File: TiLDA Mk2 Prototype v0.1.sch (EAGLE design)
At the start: 196 parts, among them IC1 ATSAM3X8EA-AU, IC10 MCP73831, IC2 MPU-6050, IC3 SRF-V1.2, IC5 S25FL216K0PMFI011, IC7 HMC5883LSMD (NP), IC8 MCP1825T-3302E/DC, IC9 TC1015-3V3, J1 ZX62-AB-5PA(11), J3 Arduino Headers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

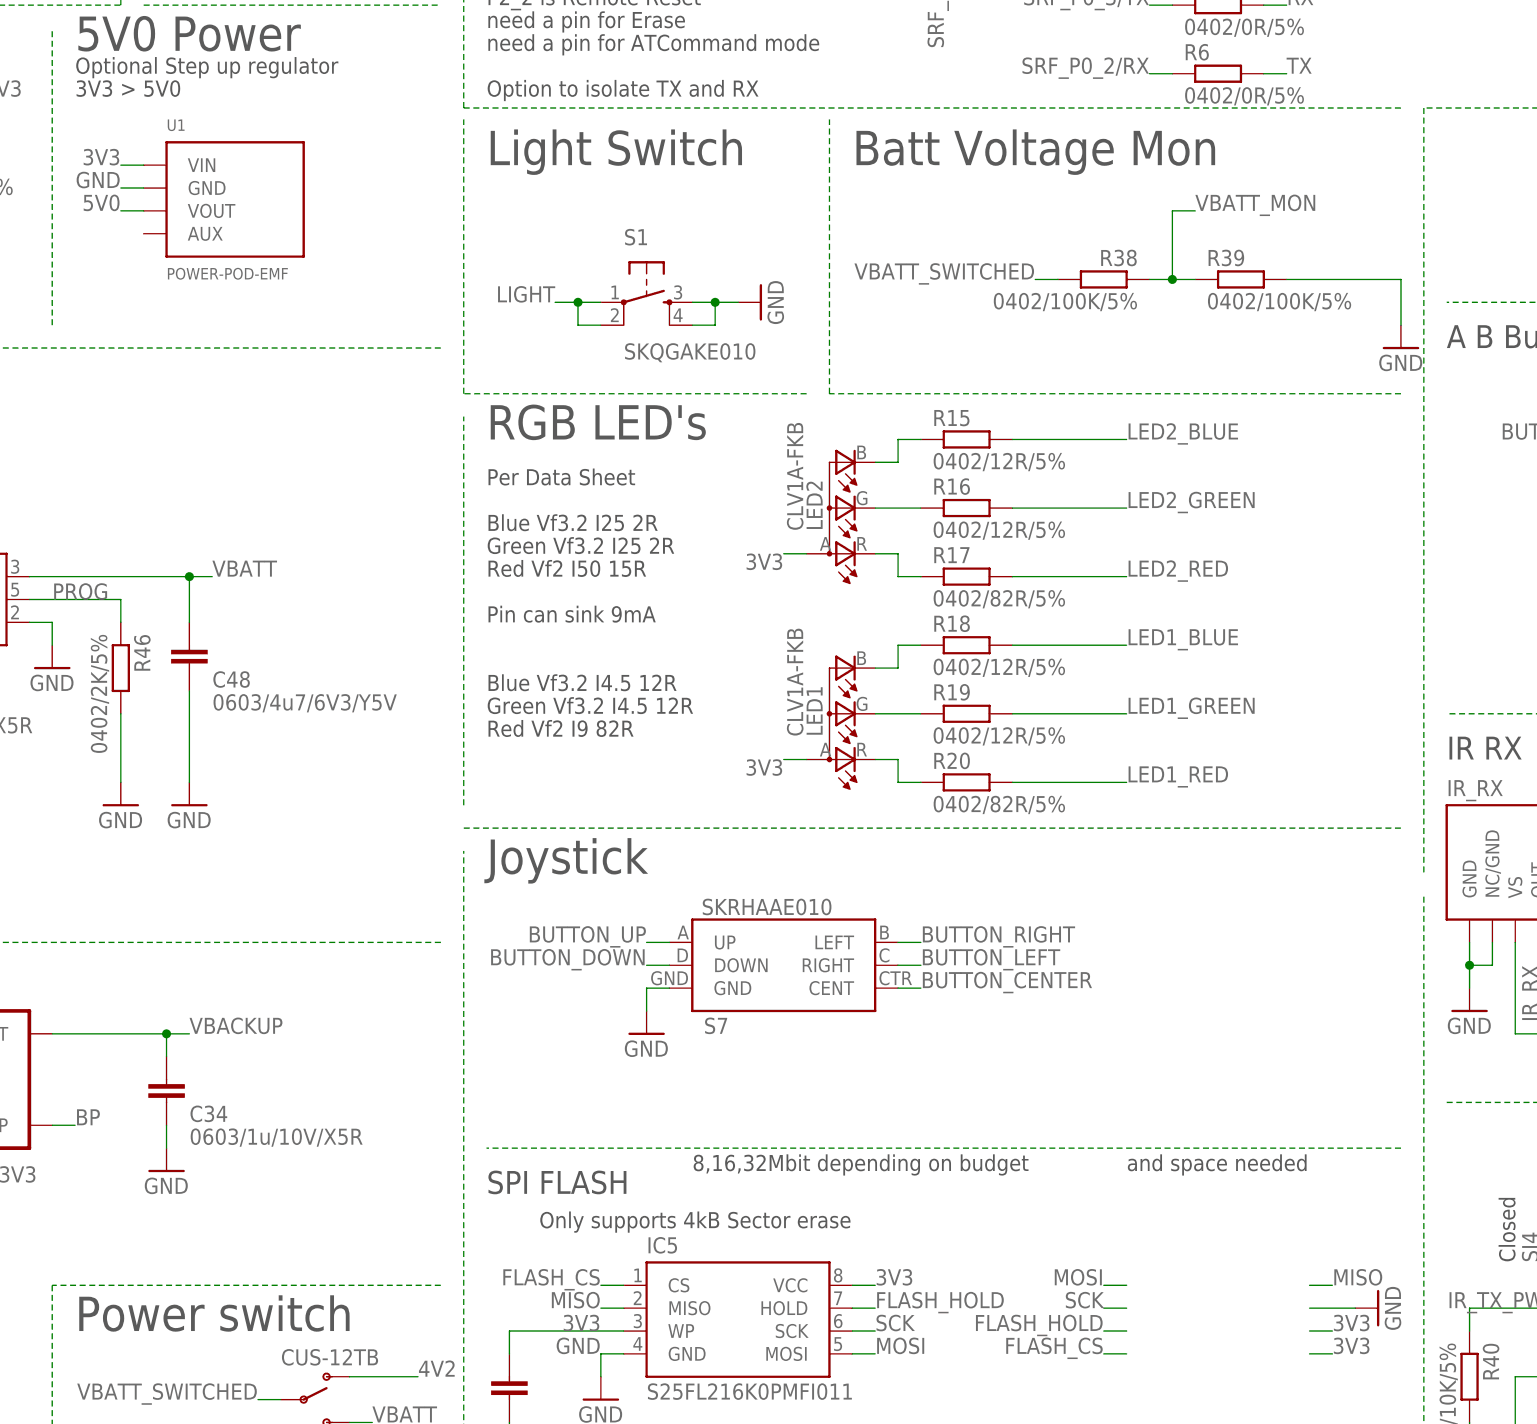
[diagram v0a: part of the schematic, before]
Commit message: Prototype: Last tweak for v0.2, adding SJ for VDDIO between 3V3 and VBACKUP
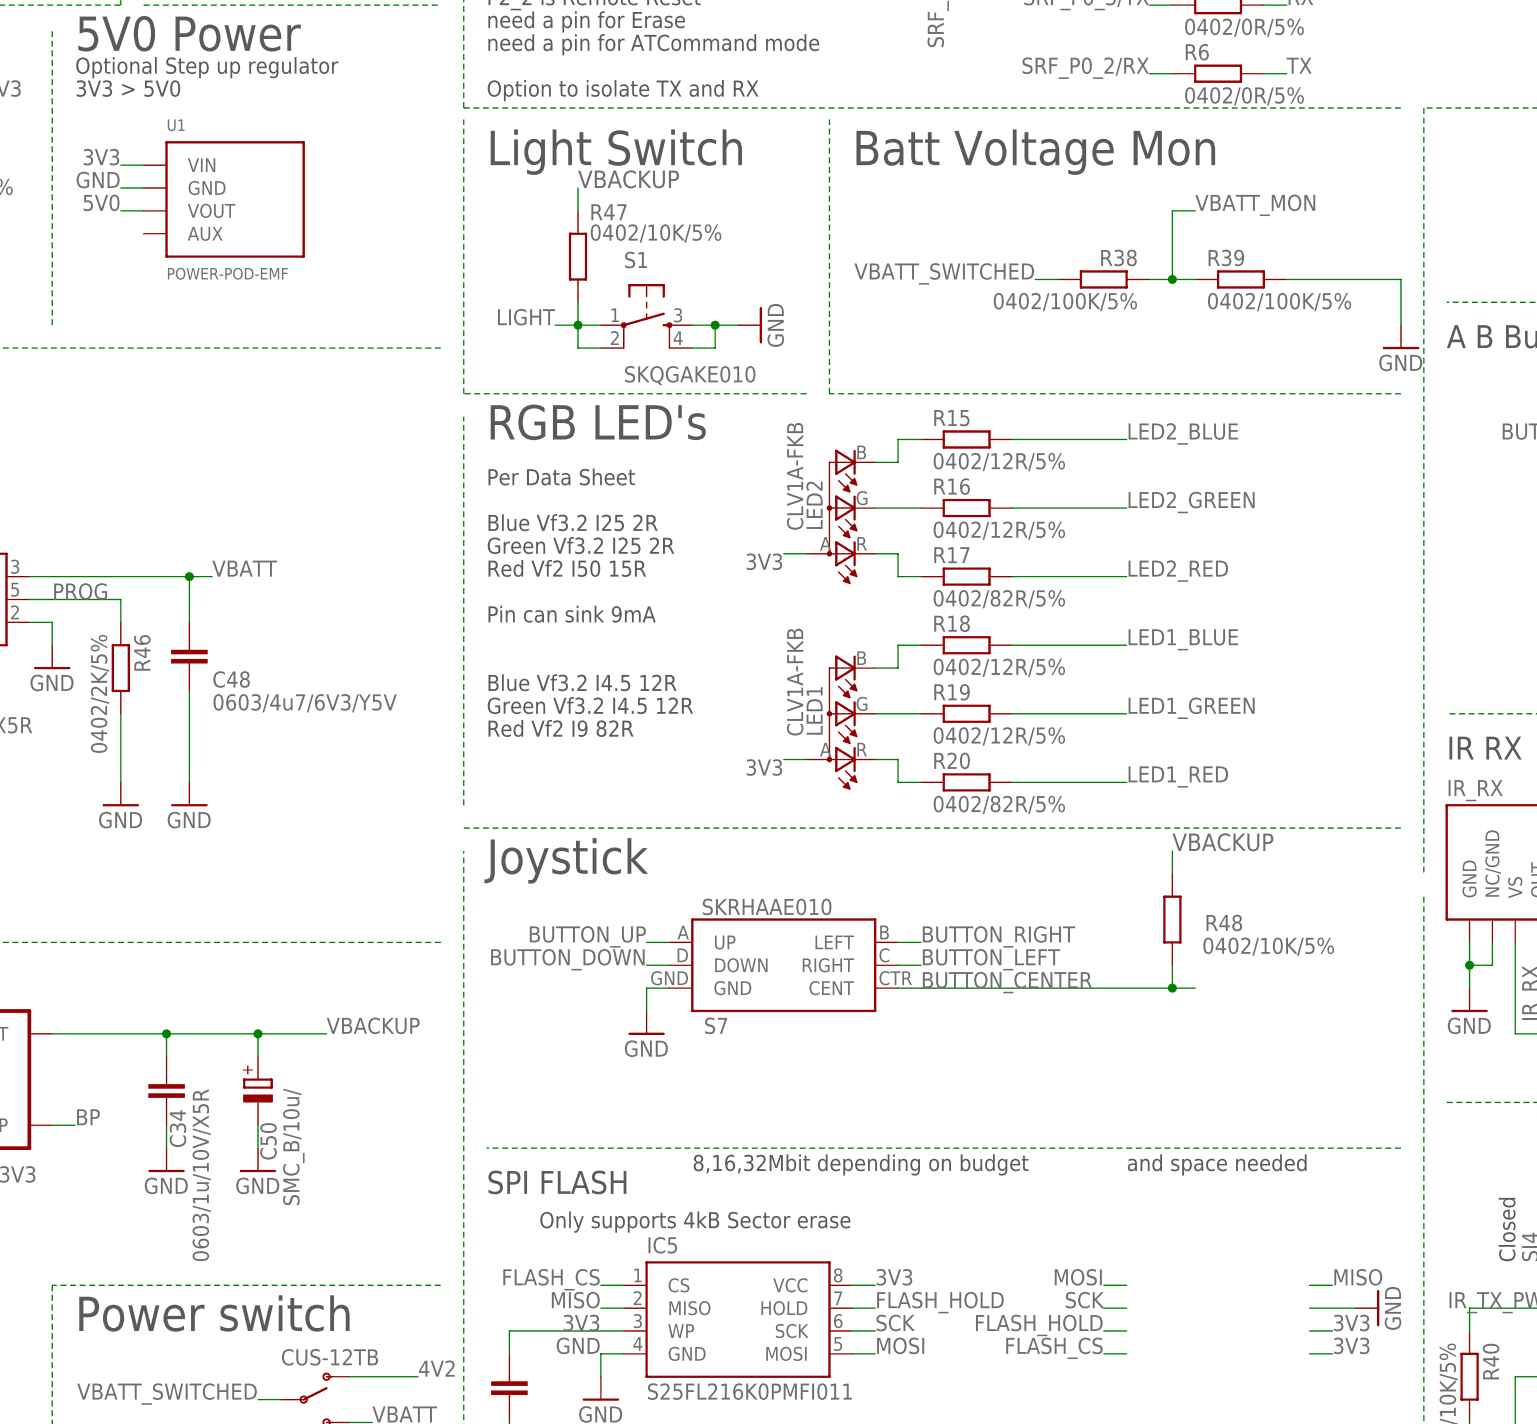
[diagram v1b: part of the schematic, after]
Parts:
- added C50: SMC_B/10u/, TiLDA Mk2 Parts:CPOL-EU-C0805RNDPOL
- added R47, R48: 0402/10K/5%, TiLDA Mk2 Parts:R-EU_R0402-ARDUINO-ROUND
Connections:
- net BUTTON_CENTER: now also R48.1
- net GND: now also C50.-
- net LIGHT: now also R47.1
- net VBACKUP: now also C50.+, R47.2, R48.2
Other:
- moved on the sheet: S1
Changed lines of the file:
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@@
 </part>
 <part name="U1" library="TiLDA Mk2 Parts" deviceset="POWER-POD" device="-EMF"/>
+<part name="R47" library="TiLDA Mk2 Parts" deviceset="R-EU_" device="R0402-ARDUINO-ROUND" value="0402/10K/5%"/>
+<part name="R48" library="TiLDA Mk2 Parts" deviceset="R-EU_" device="R0402-ARDUINO-ROUND" value="0402/10K/5%"/>
+<part name="C50" library="TiLDA Mk2 Parts" deviceset="CPOL-EU" device="-C0805RNDPOL" value="SMC_B/10u/"/>
+<part name="GND9" library="TiLDA Mk2 Parts" deviceset="GND" device=""/>
 </parts>
 <sheets>
@@
 <attribute name="VALUE" x="561.34" y="132.08" size="1.778" layer="94"/>
 </instance>
-<instance part="S1" gate="S" x="134.62" y="134.62"/>
+<instance part="S1" gate="S" x="134.62" y="132.08"/>
 <instance part="S4" gate="S" x="426.72" y="185.42"/>
 <instance part="FRAME2" gate="G$1" x="401.32" y="0"/>
@@
 </instance>
 <instance part="GND41" gate="1" x="439.42" y="185.42" rot="R90"/>
-<instance part="GND42" gate="1" x="147.32" y="134.62" rot="R90"/>
+<instance part="GND42" gate="1" x="147.32" y="132.08" rot="R90"/>
 <instance part="GND43" gate="1" x="375.92" y="121.92" rot="R90"/>
 <instance part="GND44" gate="1" x="375.92" y="106.68" rot="R90"/>
@@
 </instance>
 <instance part="C34" gate="G$1" x="81.28" y="45.72" smashed="yes" rot="R180">
-<attribute name="NAME" x="83.82" y="43.561" size="1.778" layer="95"/>
-<attribute name="VALUE" x="83.82" y="41.021" size="1.778" layer="96"/>
+<attribute name="NAME" x="83.439" y="40.64" size="1.778" layer="95" rot="R90"/>
+<attribute name="VALUE" x="85.979" y="27.94" size="1.778" layer="96" rot="R90"/>
 </instance>
 <instance part="GND63" gate="1" x="35.56" y="35.56"/>
@@
 <instance part="TP26" gate="G$1" x="670.56" y="182.88" rot="R270"/>
 <instance part="U1" gate="G$1" x="88.9" y="144.78"/>
+<instance part="R47" gate="G$1" x="127" y="139.7" smashed="yes" rot="R90">
+<attribute name="NAME" x="128.27" y="143.7386" size="1.778" layer="95"/>
+<attribute name="VALUE" x="128.27" y="141.478" size="1.778" layer="96"/>
+</instance>
+<instance part="R48" gate="G$1" x="193.04" y="66.04" smashed="yes" rot="R90">
+<attribute name="NAME" x="196.6214" y="64.77" size="1.778" layer="95"/>
+<attribute name="VALUE" x="196.342" y="62.23" size="1.778" layer="96"/>
+</instance>
+<instance part="C50" gate="G$1" x="91.44" y="48.26" smashed="yes">
+<attribute name="NAME" x="93.4974" y="39.243" size="1.778" layer="95" rot="R90"/>
+<attribute name="VALUE" x="96.0374" y="34.163" size="1.778" layer="96" rot="R90"/>
+</instance>
+<instance part="GND9" gate="1" x="91.44" y="38.1"/>
 </instances>
 <busses>
@@
 <segment>
 <pinref part="S1" gate="S" pin="3"/>
-<wire x1="139.7" y1="134.62" x2="142.24" y2="134.62" width="0.1524" layer="91"/>
-<pinref part="S1" gate="S" pin="4"/>
-<wire x1="142.24" y1="134.62" x2="144.78" y2="134.62" width="0.1524" layer="91"/>
 <wire x1="139.7" y1="132.08" x2="142.24" y2="132.08" width="0.1524" layer="91"/>
-<wire x1="142.24" y1="132.08" x2="142.24" y2="134.62" width="0.1524" layer="91"/>
-<junction x="142.24" y="134.62"/>
+<pinref part="S1" gate="S" pin="4"/>
+<wire x1="142.24" y1="132.08" x2="144.78" y2="132.08" width="0.1524" layer="91"/>
+<wire x1="139.7" y1="129.54" x2="142.24" y2="129.54" width="0.1524" layer="91"/>
+<wire x1="142.24" y1="129.54" x2="142.24" y2="132.08" width="0.1524" layer="91"/>
+<junction x="142.24" y="132.08"/>
 <pinref part="GND42" gate="1" pin="GND"/>
 </segment>
@@
 <pinref part="GND1" gate="1" pin="GND"/>
 </segment>
+<segment>
+<pinref part="C50" gate="G$1" pin="-"/>
+<pinref part="GND9" gate="1" pin="GND"/>
+<wire x1="91.44" y1="40.64" x2="91.44" y2="43.18" width="0.1524" layer="91"/>
+</segment>
 </net>
 <net name="PD10" class="0">
@@
 <segment>
 <pinref part="S1" gate="S" pin="1"/>
-<wire x1="124.46" y1="134.62" x2="127" y2="134.62" width="0.1524" layer="91"/>
-<wire x1="127" y1="134.62" x2="129.54" y2="134.62" width="0.1524" layer="91"/>
-<wire x1="127" y1="134.62" x2="127" y2="132.08" width="0.1524" layer="91"/>
-<junction x="127" y="134.62"/>
-<pinref part="S1" gate="S" pin="2"/>
+<wire x1="124.46" y1="132.08" x2="127" y2="132.08" width="0.1524" layer="91"/>
 <wire x1="127" y1="132.08" x2="129.54" y2="132.08" width="0.1524" layer="91"/>
-<label x="124.46" y="134.62" size="1.778" layer="95" rot="MR0"/>
+<wire x1="127" y1="132.08" x2="127" y2="129.54" width="0.1524" layer="91"/>
+<junction x="127" y="132.08"/>
+<pinref part="S1" gate="S" pin="2"/>
+<wire x1="127" y1="129.54" x2="129.54" y2="129.54" width="0.1524" layer="91"/>
+<label x="124.46" y="132.08" size="1.778" layer="95" rot="MR0"/>
+<pinref part="R47" gate="G$1" pin="1"/>
+<wire x1="127" y1="132.08" x2="127" y2="134.62" width="0.1524" layer="91"/>
 </segment>
 <segment>
@@
 <net name="BUTTON_CENTER" class="0">
 <segment>
-<wire x1="162.56" y1="58.42" x2="165.1" y2="58.42" width="0.1524" layer="91"/>
 <label x="165.1" y="58.42" size="1.778" layer="95"/>
 <pinref part="S7" gate="G$1" pin="CENT"/>
+<pinref part="R48" gate="G$1" pin="1"/>
+<wire x1="162.56" y1="58.42" x2="193.04" y2="58.42" width="0.1524" layer="91"/>
+<wire x1="193.04" y1="58.42" x2="193.04" y2="60.96" width="0.1524" layer="91"/>
+<wire x1="193.04" y1="58.42" x2="195.58" y2="58.42" width="0.1524" layer="91"/>
+<junction x="193.04" y="58.42"/>
 </segment>
 <segment>
@@
 <segment>
 <pinref part="C34" gate="G$1" pin="2"/>
-<wire x1="81.28" y1="53.34" x2="83.82" y2="53.34" width="0.1524" layer="91"/>
+<wire x1="81.28" y1="53.34" x2="91.44" y2="53.34" width="0.1524" layer="91"/>
+<wire x1="91.44" y1="53.34" x2="99.06" y2="53.34" width="0.1524" layer="91"/>
 <wire x1="81.28" y1="50.8" x2="81.28" y2="53.34" width="0.1524" layer="91"/>
 <pinref part="IC9" gate="G$1" pin="OUT"/>
 <wire x1="81.28" y1="53.34" x2="68.58" y2="53.34" width="0.1524" layer="91"/>
-<label x="83.82" y="53.34" size="1.778" layer="95"/>
+<label x="99.06" y="53.34" size="1.778" layer="95"/>
 <junction x="81.28" y="53.34"/>
+<pinref part="C50" gate="G$1" pin="+"/>
+<wire x1="91.44" y1="53.34" x2="91.44" y2="50.8" width="0.1524" layer="91"/>
+<junction x="91.44" y="53.34"/>
 </segment>
 <segment>
@@
 <label x="741.68" y="149.86" size="1.778" layer="95" rot="R90"/>
 </segment>
+<segment>
+<pinref part="R47" gate="G$1" pin="2"/>
+<wire x1="127" y1="144.78" x2="127" y2="147.32" width="0.1524" layer="91"/>
+<label x="127" y="147.32" size="1.9304" layer="95"/>
+</segment>
+<segment>
+<pinref part="R48" gate="G$1" pin="2"/>
+<wire x1="193.04" y1="71.12" x2="193.04" y2="73.66" width="0.1524" layer="91"/>
+<label x="193.04" y="73.66" size="1.9304" layer="95"/>
+</segment>
 </net>
